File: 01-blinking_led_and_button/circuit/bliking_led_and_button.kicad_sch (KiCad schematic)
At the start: 5 parts, among them SW1 SW_SPST

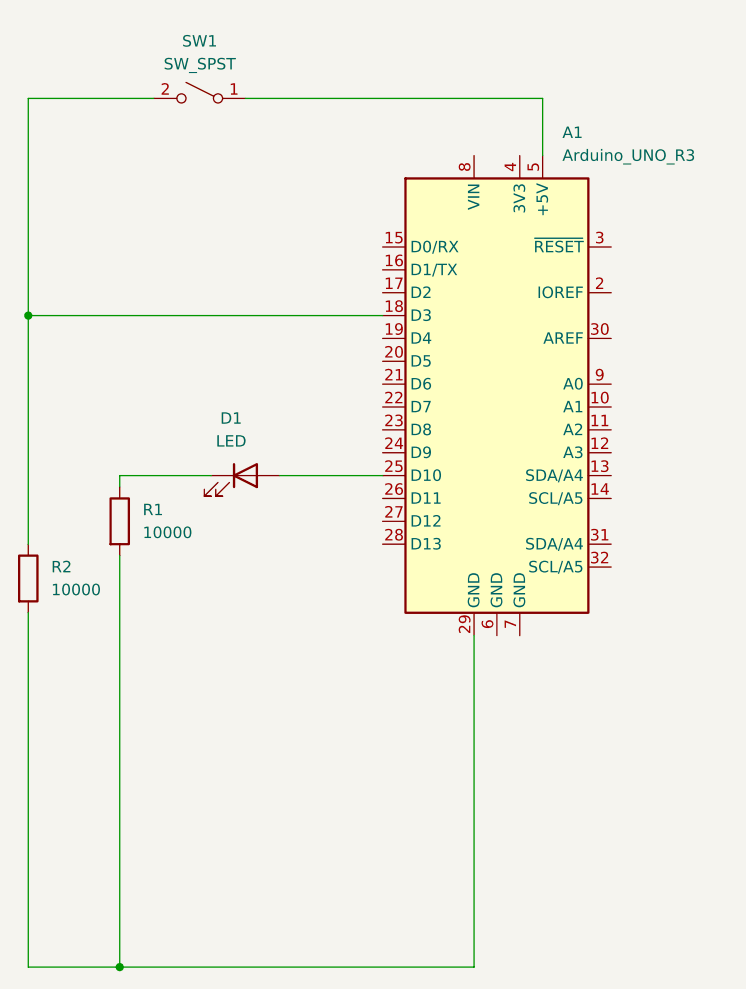
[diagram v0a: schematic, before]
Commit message: FIX change the normal switch button to a tactile switch
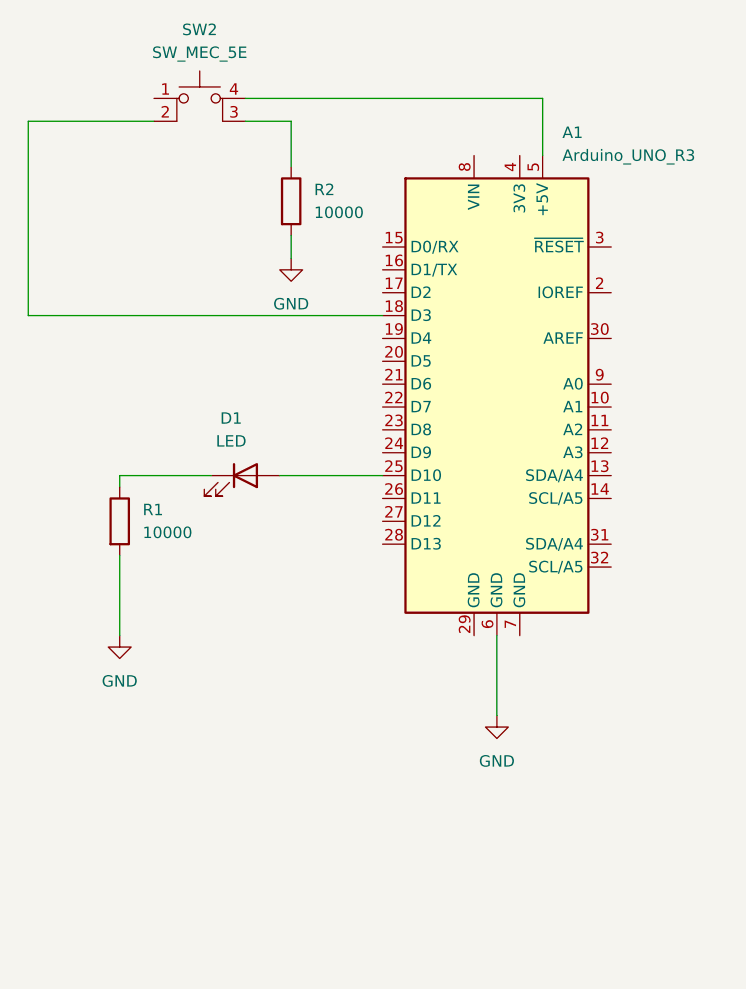
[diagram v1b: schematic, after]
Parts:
- removed SW1: SW_SPST, symbol Switch:SW_SPST
- added SW2: SW_MEC_5E, symbol Switch:SW_MEC_5E
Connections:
- net at R2.1: now also SW2.3 (K); no longer A1.18 (D3)
- net GND: now reaches R1.2, R2.2
- net GND: now also A1.6 (GND); no longer A1.29 (GND)
- net at A1.5 (+5V): now also SW2.4 (A)
- new net: A1.18 (D3), SW2.2
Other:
- moved on the sheet: R2
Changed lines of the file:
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@@
 (kicad_sch (version 20230121) (generator eeschema)
   (paper "A4")
-  (junction (at 127 63.5) (diameter 0) (color 0 0 0 0)
-  )
-  (junction (at 137.16 135.89) (diameter 0) (color 0 0 0 0)
-  )
-  (wire (pts (xy 127 96.52) (xy 127 135.89))
-    (stroke (width 0) (type default))
-  )
   (wire (pts (xy 154.94 81.28) (xy 166.37 81.28))
     (stroke (width 0) (type default))
   )
-  (wire (pts (xy 140.97 39.37) (xy 127 39.37))
+  (wire (pts (xy 156.21 41.91) (xy 156.21 46.99))
+    (stroke (width 0) (type default))
+  )
+  (wire (pts (xy 127 41.91) (xy 127 63.5))
     (stroke (width 0) (type default))
   )
@@
     (stroke (width 0) (type default))
   )
-  (wire (pts (xy 127 63.5) (xy 127 88.9))
-    (stroke (width 0) (type default))
-  )
-  (wire (pts (xy 176.53 135.89) (xy 176.53 99.06))
-    (stroke (width 0) (type default))
-  )
   (wire (pts (xy 184.15 45.72) (xy 184.15 39.37))
     (stroke (width 0) (type default))
   )
-  (wire (pts (xy 127 39.37) (xy 127 63.5))
-    (stroke (width 0) (type default))
-  )
-  (wire (pts (xy 137.16 135.89) (xy 176.53 135.89))
-    (stroke (width 0) (type default))
-  )
-  (wire (pts (xy 127 135.89) (xy 137.16 135.89))
+  (wire (pts (xy 137.16 90.17) (xy 137.16 99.06))
+    (stroke (width 0) (type default))
+  )
+  (wire (pts (xy 179.07 99.06) (xy 179.07 107.95))
     (stroke (width 0) (type default))
   )
@@
     (stroke (width 0) (type default))
   )
+  (wire (pts (xy 151.13 41.91) (xy 156.21 41.91))
+    (stroke (width 0) (type default))
+  )
+  (wire (pts (xy 127 41.91) (xy 140.97 41.91))
+    (stroke (width 0) (type default))
+  )
   (wire (pts (xy 127 63.5) (xy 166.37 63.5))
     (stroke (width 0) (type default))
   )
+  (wire (pts (xy 156.21 54.61) (xy 156.21 57.15))
+    (stroke (width 0) (type default))
+  )
   (wire (pts (xy 137.16 81.28) (xy 147.32 81.28))
     (stroke (width 0) (type default))
   )
-  (wire (pts (xy 137.16 90.17) (xy 137.16 135.89))
-    (stroke (width 0) (type default))
-  )
-  (symbol (lib_id "Device:R") (at 127 92.71 0) (unit 1)
-    (in_bom yes) (on_board yes) (dnp no) (fields_autoplaced)
-    (property "Reference" "R2" (at 129.54 91.44 0)
-      (effects (font (size 1.27 1.27)) (justify left))
-    )
-    (property "Value" "10000" (at 129.54 93.98 0)
-      (effects (font (size 1.27 1.27)) (justify left))
-    )
-    (property "Footprint" "" (at 125.222 92.71 90)
-      (effects (font (size 1.27 1.27)) hide)
-    )
-    (property "Datasheet" "~" (at 127 92.71 0)
+  (symbol (lib_id "Device:R") (at 156.21 50.8 0) (unit 1)
+    (in_bom yes) (on_board yes) (dnp no) (fields_autoplaced)
+    (property "Reference" "R2" (at 158.75 49.53 0)
+      (effects (font (size 1.27 1.27)) (justify left))
+    )
+    (property "Value" "10000" (at 158.75 52.07 0)
+      (effects (font (size 1.27 1.27)) (justify left))
+    )
+    (property "Footprint" "" (at 154.432 50.8 90)
+      (effects (font (size 1.27 1.27)) hide)
+    )
+    (property "Datasheet" "~" (at 156.21 50.8 0)
       (effects (font (size 1.27 1.27)) hide)
     )
@@
     )
   )
+  (symbol (lib_id "power:GND") (at 156.21 57.15 0) (unit 1)
+    (in_bom yes) (on_board yes) (dnp no) (fields_autoplaced)
+    (property "Reference" "#PWR03" (at 156.21 63.5 0)
+      (effects (font (size 1.27 1.27)) hide)
+    )
+    (property "Value" "GND" (at 156.21 62.23 0)
+      (effects (font (size 1.27 1.27)))
+    )
+    (property "Footprint" "" (at 156.21 57.15 0)
+      (effects (font (size 1.27 1.27)) hide)
+    )
+    (property "Datasheet" "" (at 156.21 57.15 0)
+      (effects (font (size 1.27 1.27)) hide)
+    )
+    (pin "1")
+    (instances
+      (project "bliking_led_and_button"
+        (path "/8113053d-624a-40b5-9d0c-1205b7866605"
+          (reference "#PWR03") (unit 1)
+        )
+      )
+    )
+  )
   (symbol (lib_id "Device:R") (at 137.16 86.36 0) (unit 1)
     (in_bom yes) (on_board yes) (dnp no) (fields_autoplaced)
@@
         (path "/8113053d-624a-40b5-9d0c-1205b7866605"
           (reference "R1") (unit 1)
+        )
+      )
+    )
+  )
+  (symbol (lib_id "Switch:SW_MEC_5E") (at 146.05 41.91 0) (unit 1)
+    (in_bom yes) (on_board yes) (dnp no) (fields_autoplaced)
+    (property "Reference" "SW2" (at 146.05 31.75 0)
+      (effects (font (size 1.27 1.27)))
+    )
+    (property "Value" "SW_MEC_5E" (at 146.05 34.29 0)
+      (effects (font (size 1.27 1.27)))
+    )
+    (property "Footprint" "" (at 146.05 34.29 0)
+      (effects (font (size 1.27 1.27)) hide)
+    )
+    (property "Datasheet" "http://www.apem.com/int/index.php?controller=attachment&id_attachment=1371" (at 146.05 34.29 0)
+      (effects (font (size 1.27 1.27)) hide)
+    )
+    (pin "3")
+    (pin "4")
+    (pin "1")
+    (pin "2")
+    (instances
+      (project "bliking_led_and_button"
+        (path "/8113053d-624a-40b5-9d0c-1205b7866605"
+          (reference "SW2") (unit 1)
+        )
+      )
+    )
+  )
+  (symbol (lib_id "power:GND") (at 137.16 99.06 0) (unit 1)
+    (in_bom yes) (on_board yes) (dnp no) (fields_autoplaced)
+    (property "Reference" "#PWR02" (at 137.16 105.41 0)
+      (effects (font (size 1.27 1.27)) hide)
+    )
+    (property "Value" "GND" (at 137.16 104.14 0)
+      (effects (font (size 1.27 1.27)))
+    )
+    (property "Footprint" "" (at 137.16 99.06 0)
+      (effects (font (size 1.27 1.27)) hide)
+    )
+    (property "Datasheet" "" (at 137.16 99.06 0)
+      (effects (font (size 1.27 1.27)) hide)
+    )
+    (pin "1")
+    (instances
+      (project "bliking_led_and_button"
+        (path "/8113053d-624a-40b5-9d0c-1205b7866605"
+          (reference "#PWR02") (unit 1)
         )
       )
@@
     )
   )
-  (symbol (lib_id "Switch:SW_SPST") (at 146.05 39.37 0) (mirror y) (unit 1)
-    (in_bom yes) (on_board yes) (dnp no)
-    (property "Reference" "SW1" (at 146.05 33.02 0)
-      (effects (font (size 1.27 1.27)))
-    )
-    (property "Value" "SW_SPST" (at 146.05 35.56 0)
-      (effects (font (size 1.27 1.27)))
-    )
-    (property "Footprint" "" (at 146.05 39.37 0)
-      (effects (font (size 1.27 1.27)) hide)
-    )
-    (property "Datasheet" "~" (at 146.05 39.37 0)
-      (effects (font (size 1.27 1.27)) hide)
-    )
-    (pin "1")
-    (pin "2")
-    (instances
-      (project "bliking_led_and_button"
-        (path "/8113053d-624a-40b5-9d0c-1205b7866605"
-          (reference "SW1") (unit 1)
-        )
-      )
+  (symbol (lib_id "power:GND") (at 179.07 107.95 0) (unit 1)
+    (in_bom yes) (on_board yes) (dnp no) (fields_autoplaced)
+    (property "Reference" "#PWR01" (at 179.07 114.3 0)
+      (effects (font (size 1.27 1.27)) hide)
+    )
+    (property "Value" "GND" (at 179.07 113.03 0)
+      (effects (font (size 1.27 1.27)))
+    )
+    (property "Footprint" "" (at 179.07 107.95 0)
+      (effects (font (size 1.27 1.27)) hide)
+    )
+    (property "Datasheet" "" (at 179.07 107.95 0)
+      (effects (font (size 1.27 1.27)) hide)
+    )
+    (pin "1")
+    (instances
+      (project "bliking_led_and_button"
+        (path "/8113053d-624a-40b5-9d0c-1205b7866605"
+          (reference "#PWR01") (unit 1)
+        )
+      )
